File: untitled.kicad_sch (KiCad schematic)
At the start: 16 parts, among them IC1 MIC5528-3.3YMT-T5, J1 LiPo Battery, J2 USB_B_Micro, Q1 FDN340P, U1 USBLC6-2SC6, U2 MCP73831-2-OT

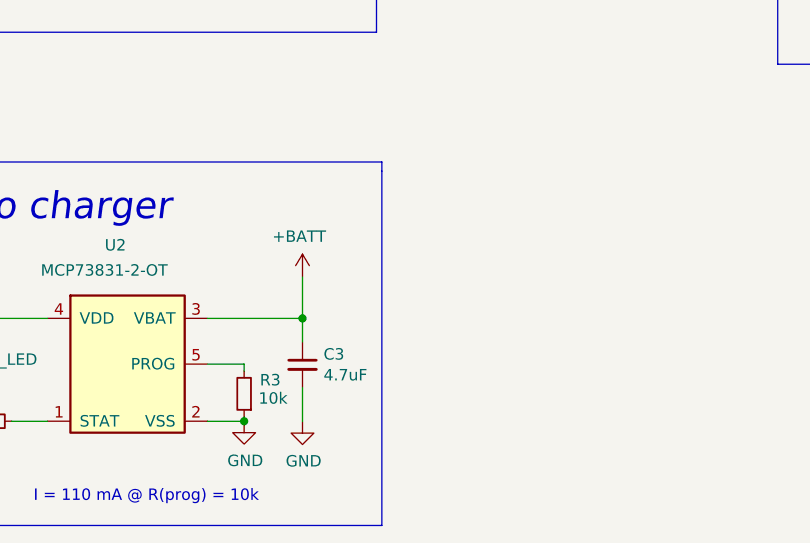
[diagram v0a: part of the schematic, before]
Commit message: Made new layout
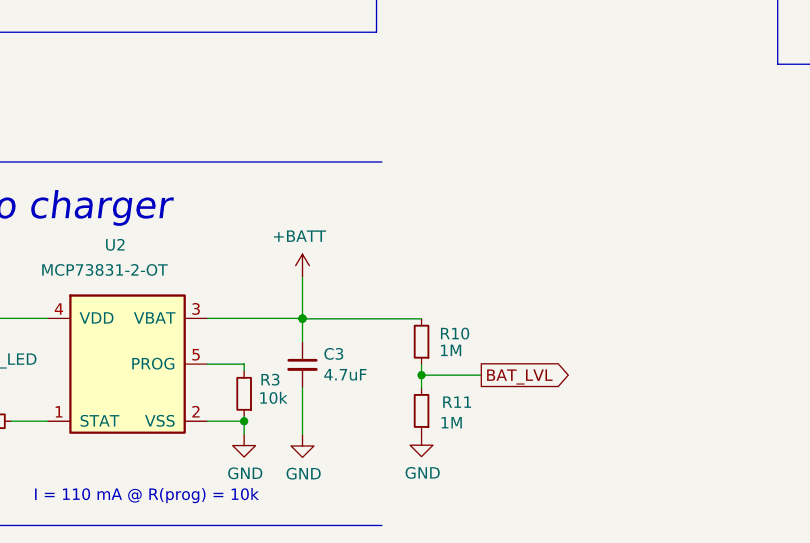
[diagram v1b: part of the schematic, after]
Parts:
- added R10, R11: 1M, Resistor_SMD:R_0402_1005Metric, symbol Device:R_Small
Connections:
- net +BATT: now also R10.2
- net GND: now also R11.1
- new net BAT_LVL: R10.1, R11.2
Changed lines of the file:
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@@
 (kicad_sch (version 20211123) (generator eeschema)
   (paper "A4")
+  (junction (at 129.1011 74.168) (diameter 0) (color 0 0 0 0)
+  )
+  (junction (at 204.6564 74.168) (diameter 0) (color 0 0 0 0)
+  )
+  (junction (at 121.3038 128.3142) (diameter 0) (color 0 0 0 0)
+  )
+  (junction (at 148.5222 43.9443) (diameter 0) (color 0 0 0 0)
+  )
+  (junction (at 148.5222 74.168) (diameter 0) (color 0 0 0 0)
+  )
+  (junction (at 173.3875 128.3641) (diameter 0) (color 0 0 0 0)
+  )
+  (junction (at 186.6148 134.6228) (diameter 0) (color 0 0 0 0)
+  )
+  (junction (at 121.3038 128.4116) (diameter 0) (color 0 0 0 0)
+  )
+  (junction (at 121.3038 65.532) (diameter 0) (color 0 0 0 0)
+  )
+  (junction (at 129.1011 65.532) (diameter 0) (color 0 0 0 0)
+  )
+  (junction (at 255.2598 74.168) (diameter 0) (color 0 0 0 0)
+  )
   (junction (at 166.9021 139.7442) (diameter 0) (color 0 0 0 0)
-  )
-  (junction (at 129.1011 74.168) (diameter 0) (color 0 0 0 0)
-  )
-  (junction (at 204.6564 74.168) (diameter 0) (color 0 0 0 0)
-  )
-  (junction (at 121.3038 128.3142) (diameter 0) (color 0 0 0 0)
-  )
-  (junction (at 148.5222 43.9443) (diameter 0) (color 0 0 0 0)
-  )
-  (junction (at 148.5222 74.168) (diameter 0) (color 0 0 0 0)
-  )
-  (junction (at 121.3038 128.4116) (diameter 0) (color 0 0 0 0)
-  )
-  (junction (at 121.3038 65.532) (diameter 0) (color 0 0 0 0)
-  )
-  (junction (at 129.1011 65.532) (diameter 0) (color 0 0 0 0)
-  )
-  (junction (at 255.2598 74.168) (diameter 0) (color 0 0 0 0)
   )
   (junction (at 268.7258 74.168) (diameter 0) (color 0 0 0 0)
@@
     (stroke (width 0) (type default) (color 0 0 0 0))
   )
+  (wire (pts (xy 173.3875 128.3641) (xy 173.3875 130.935))
+    (stroke (width 0) (type default) (color 0 0 0 0))
+  )
   (polyline (pts (xy 182.2048 151.324) (xy 115.1488 151.324))
     (stroke (width 0) (type default) (color 0 0 0 0))
@@
     (stroke (width 0) (type default) (color 0 0 0 0))
   )
+  (wire (pts (xy 166.9021 139.7442) (xy 166.9021 141.1783))
+    (stroke (width 0) (type default) (color 0 0 0 0))
+  )
   (polyline (pts (xy 18.0111 53.594) (xy 100.5611 53.594))
     (stroke (width 0) (type default) (color 0 0 0 0))
@@
     (stroke (width 0) (type default) (color 0 0 0 0))
   )
+  (wire (pts (xy 193.2519 134.6228) (xy 186.6148 134.6228))
+    (stroke (width 0) (type default) (color 0 0 0 0))
+  )
   (polyline (pts (xy 100.5611 106.934) (xy 18.0111 106.934))
     (stroke (width 0) (type default) (color 0 0 0 0))
@@
     (stroke (width 0) (type default) (color 0 0 0 0))
   )
+  (wire (pts (xy 186.6148 134.6228) (xy 186.6148 136.0556))
+    (stroke (width 0) (type default) (color 0 0 0 0))
+  )
   (wire (pts (xy 129.1011 83.82) (xy 129.1011 88.5206))
     (stroke (width 0) (type default) (color 0 0 0 0))
@@
     (stroke (width 0) (type default) (color 0 0 0 0))
   )
-  (polyline (pts (xy 182.2048 110.938) (xy 182.2048 111.954))
+  (wire (pts (xy 186.6148 133.4441) (xy 186.6148 134.6228))
     (stroke (width 0) (type default) (color 0 0 0 0))
   )
@@
     (stroke (width 0) (type default) (color 0 0 0 0))
   )
+  (wire (pts (xy 186.6148 128.3641) (xy 173.3875 128.3641))
+    (stroke (width 0) (type default) (color 0 0 0 0))
+  )
   (polyline (pts (xy 226.1878 91.44) (xy 197.4858 91.44))
     (stroke (width 0) (type default) (color 0 0 0 0))
@@
     (stroke (width 0) (type default) (color 0 0 0 0))
   )
-  (wire (pts (xy 173.3875 128.3142) (xy 173.3875 130.935))
+  (wire (pts (xy 173.3875 128.3142) (xy 173.3875 128.3641))
     (stroke (width 0) (type default) (color 0 0 0 0))
   )
@@
     (stroke (width 0) (type default) (color 0 0 0 0))
   )
-  (wire (pts (xy 173.3875 136.015) (xy 173.3875 139.7899))
+  (wire (pts (xy 173.3875 136.015) (xy 173.3875 141.224))
     (stroke (width 0) (type default) (color 0 0 0 0))
   )
   (wire (pts (xy 74.422 84.074) (xy 72.644 84.074))
-    (stroke (width 0) (type default) (color 0 0 0 0))
-  )
-  (polyline (pts (xy 182.2048 111.954) (xy 182.2048 151.324))
     (stroke (width 0) (type default) (color 0 0 0 0))
   )
@@
   (label "D+" (at 44.196 73.152 0)
     (effects (font (size 1.27 1.27)) (justify left bottom))
+  )
+  (global_label "BAT_LVL" (shape output) (at 193.2519 134.6228 0) (fields_autoplaced)
+    (effects (font (size 1.27 1.27)) (justify left))
+    (property "Intersheet References" "${INTERSHEET_REFS}" (id 0) (at 203.0147 134.5434 0)
+      (effects (font (size 1.27 1.27)) (justify left) hide)
+    )
   )
   (global_label "USBLC_D+" (shape bidirectional) (at 75.692 94.234 0) (fields_autoplaced)
@@
     (pin "1")
   )
+  (symbol (lib_id "Device:R_Small") (at 186.6148 130.9041 180) (unit 1)
+    (in_bom yes) (on_board yes)
+    (property "Reference" "R10" (id 0) (at 192.024 130.048 0)
+      (effects (font (size 1.27 1.27)) (justify left))
+    )
+    (property "Value" "1M" (id 1) (at 191.1868 131.9201 0)
+      (effects (font (size 1.27 1.27)) (justify left))
+    )
+    (property "Footprint" "Resistor_SMD:R_0402_1005Metric" (id 2) (at 186.6148 130.9041 0)
+      (effects (font (size 1.27 1.27)) hide)
+    )
+    (property "Datasheet" "~" (id 3) (at 186.6148 130.9041 0)
+      (effects (font (size 1.27 1.27)) hide)
+    )
+    (pin "1")
+    (pin "2")
+  )
   (symbol (lib_id "power:GND") (at 252.5196 85.0381 0) (mirror y) (unit 1)
     (in_bom yes) (on_board yes)
@@
     (pin "2")
   )
-  (symbol (lib_id "power:GND") (at 173.3875 139.7899 0) (unit 1)
-    (in_bom yes) (on_board yes)
-    (property "Reference" "#PWR015" (id 0) (at 173.3875 146.1399 0)
-      (effects (font (size 1.27 1.27)) hide)
-    )
-    (property "Value" "GND" (id 1) (at 173.5145 144.1841 0))
-    (property "Footprint" "" (id 2) (at 173.3875 139.7899 0)
-      (effects (font (size 1.27 1.27)) hide)
-    )
-    (property "Datasheet" "" (id 3) (at 173.3875 139.7899 0)
+  (symbol (lib_id "power:GND") (at 173.3875 141.224 0) (unit 1)
+    (in_bom yes) (on_board yes)
+    (property "Reference" "#PWR015" (id 0) (at 173.3875 147.574 0)
+      (effects (font (size 1.27 1.27)) hide)
+    )
+    (property "Value" "GND" (id 1) (at 173.5145 145.6182 0))
+    (property "Footprint" "" (id 2) (at 173.3875 141.224 0)
+      (effects (font (size 1.27 1.27)) hide)
+    )
+    (property "Datasheet" "" (id 3) (at 173.3875 141.224 0)
+      (effects (font (size 1.27 1.27)) hide)
+    )
+    (pin "1")
+  )
+  (symbol (lib_id "power:GND") (at 186.6148 141.1356 0) (unit 1)
+    (in_bom yes) (on_board yes)
+    (property "Reference" "#PWR0107" (id 0) (at 186.6148 147.4856 0)
+      (effects (font (size 1.27 1.27)) hide)
+    )
+    (property "Value" "GND" (id 1) (at 186.7418 145.5298 0))
+    (property "Footprint" "" (id 2) (at 186.6148 141.1356 0)
+      (effects (font (size 1.27 1.27)) hide)
+    )
+    (property "Datasheet" "" (id 3) (at 186.6148 141.1356 0)
       (effects (font (size 1.27 1.27)) hide)
     )
@@
     (pin "1")
   )
-  (symbol (lib_id "power:GND") (at 166.9021 139.7442 0) (unit 1)
-    (in_bom yes) (on_board yes)
-    (property "Reference" "#PWR014" (id 0) (at 166.9021 146.0942 0)
-      (effects (font (size 1.27 1.27)) hide)
-    )
-    (property "Value" "GND" (id 1) (at 167.0291 144.1384 0))
-    (property "Footprint" "" (id 2) (at 166.9021 139.7442 0)
-      (effects (font (size 1.27 1.27)) hide)
-    )
-    (property "Datasheet" "" (id 3) (at 166.9021 139.7442 0)
+  (symbol (lib_id "power:GND") (at 166.9021 141.1783 0) (unit 1)
+    (in_bom yes) (on_board yes)
+    (property "Reference" "#PWR014" (id 0) (at 166.9021 147.5283 0)
+      (effects (font (size 1.27 1.27)) hide)
+    )
+    (property "Value" "GND" (id 1) (at 167.0291 145.5725 0))
+    (property "Footprint" "" (id 2) (at 166.9021 141.1783 0)
+      (effects (font (size 1.27 1.27)) hide)
+    )
+    (property "Datasheet" "" (id 3) (at 166.9021 141.1783 0)
       (effects (font (size 1.27 1.27)) hide)
     )
@@
       (effects (font (size 1.27 1.27)) hide)
     )
+    (pin "1")
+    (pin "2")
+  )
+  (symbol (lib_id "Device:R_Small") (at 186.6148 138.5956 180) (unit 1)
+    (in_bom yes) (on_board yes)
+    (property "Reference" "R11" (id 0) (at 192.278 137.668 0)
+      (effects (font (size 1.27 1.27)) (justify left))
+    )
+    (property "Value" "1M" (id 1) (at 191.262 139.954 0)
+      (effects (font (size 1.27 1.27)) (justify left))
+    )
+    (property "Footprint" "Resistor_SMD:R_0402_1005Metric" (id 2) (at 186.6148 138.5956 0)
+      (effects (font (size 1.27 1.27)) hide)
+    )
+    (property "Datasheet" "~" (id 3) (at 186.6148 138.5956 0)
+      (effects (font (size 1.27 1.27)) hide)
+    )
